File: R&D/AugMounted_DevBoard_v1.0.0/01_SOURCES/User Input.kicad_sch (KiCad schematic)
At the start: 25 parts, among them J501 J_0788641001_PAD, J502 J_0788641001, J503 J_0788641001, J504 J_0788641001_PAD, SW501 SW_SKRTLAE010, U502 ICS‐41350

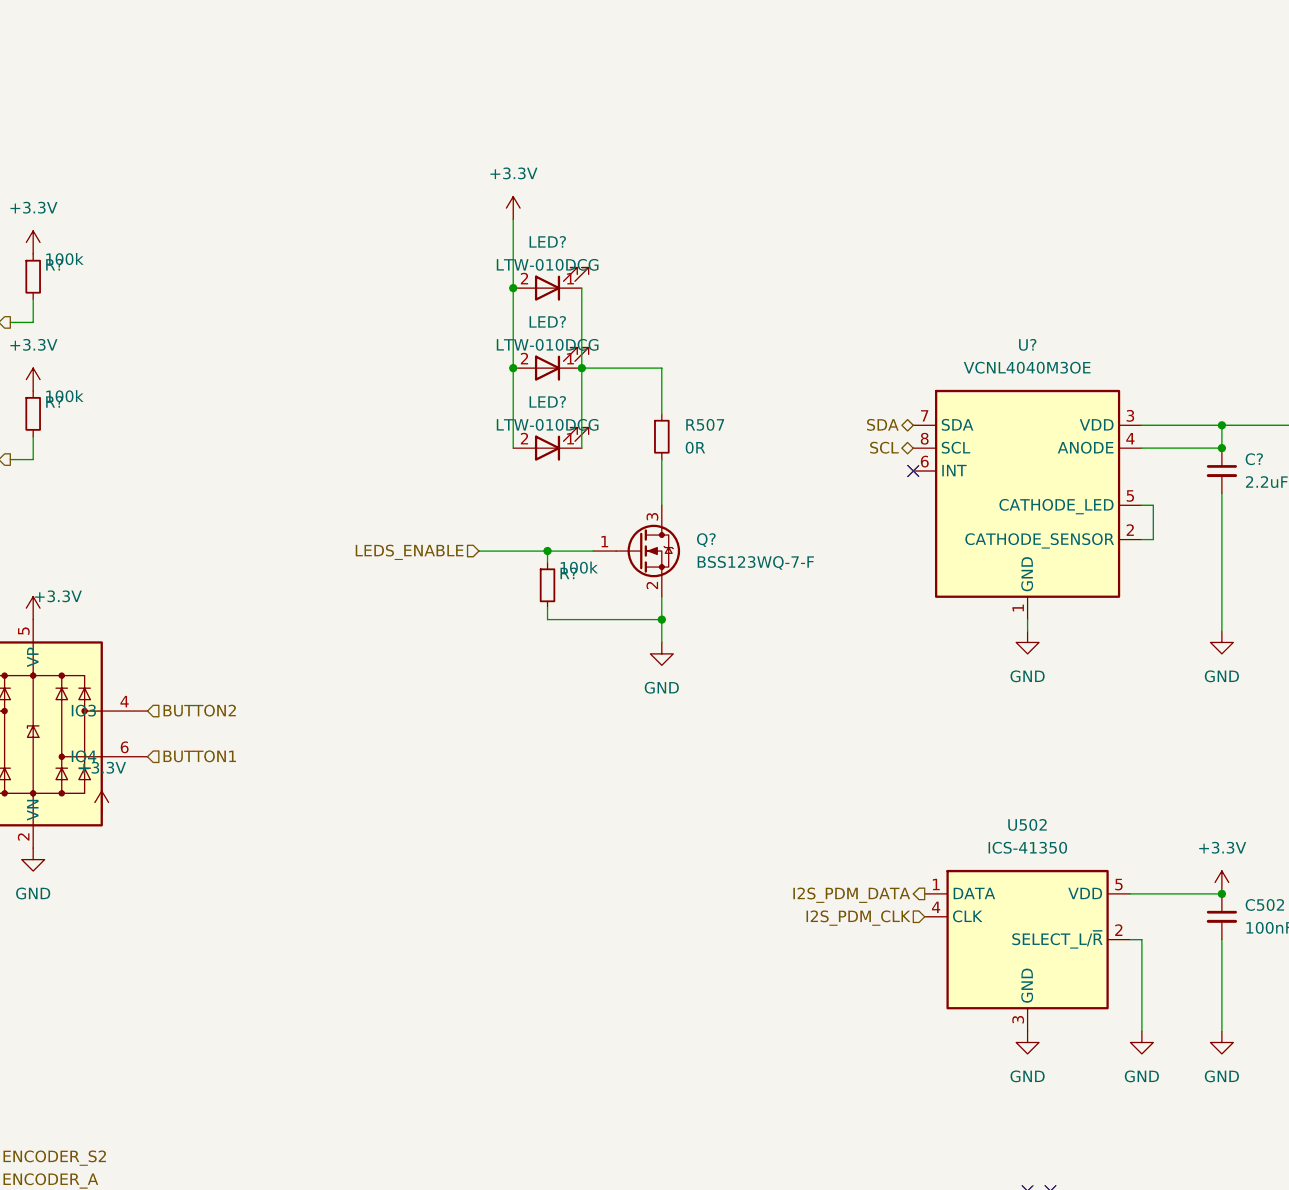
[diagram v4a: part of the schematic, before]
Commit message: Component layout is done, routing video signals is done too.
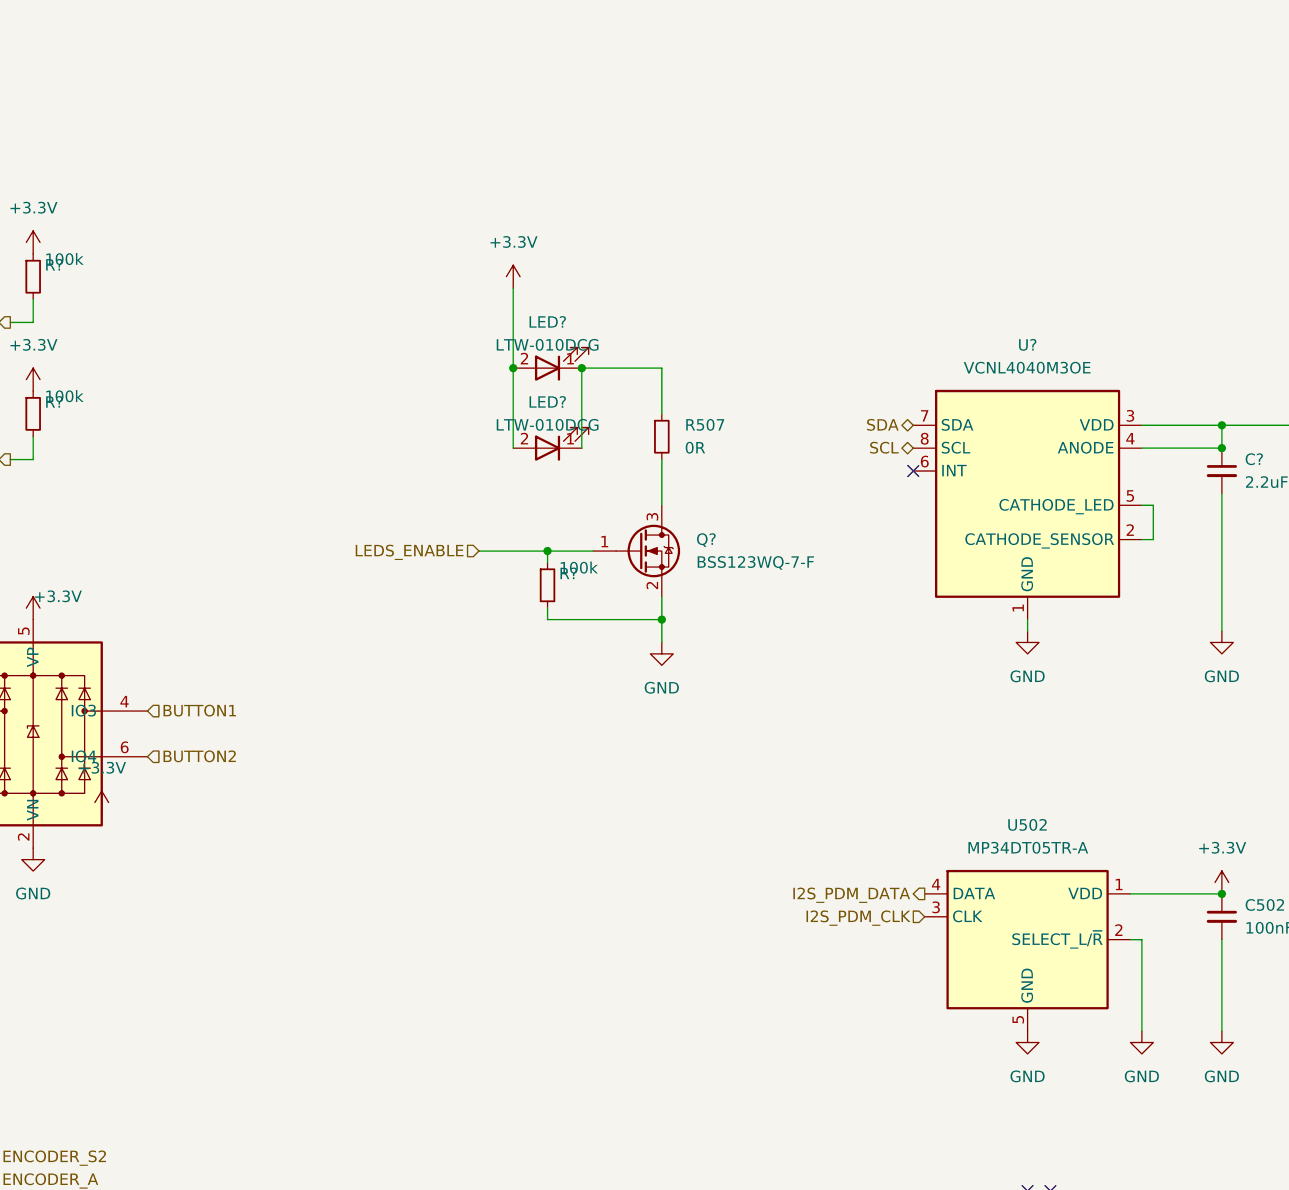
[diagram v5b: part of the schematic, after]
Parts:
- removed LED?: LED_LTW-010DCG, .mounted-lib:LED_LTW-010DCG, symbol .mounted-lib:LED_LTW-010DCG
- U502: value ICS‐41350 -> MP34DT05TR-A; footprint .mounted-lib:U_ICS-41350 -> .mounted-lib:U_MP34DT05TR-A; symbol .mounted-lib:U_ICS‐41350 -> .mounted-lib:U_MP34DT05TR-A; DisplayValue ICS‐41350 -> MP34DT05TR-A; MPN ICS‐41350 -> MP34DT05TR-A; Manufacturer TDK -> ST; MaxHeight_mm 0.98mm -> 1mm; Package ICS -> HCLGA
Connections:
- net +3.3V: now also U502.1 (VDD); no longer U502.5 (VDD)
- net BUTTON1: now also D502.4 (IO3); no longer D502.6 (IO4)
- net BUTTON2: now also D502.6 (IO4); no longer D502.4 (IO3)
- net GND: now also U502.5 (GND); no longer U502.3 (GND)
- net I2S_PDM_CLK: now also U502.3 (CLK); no longer U502.4 (CLK)
- net I2S_PDM_DATA: now also U502.4 (DATA); no longer U502.1 (DATA)
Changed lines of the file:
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@@
   (junction (at 234.95 139.7) (diameter 0) (color 0 0 0 0)
-  )
-  (junction (at 153.67 33.02) (diameter 0) (color 0 0 0 0)
   )
   (junction (at 212.09 158.75) (diameter 0) (color 0 0 0 0)
@@
     (stroke (width 0) (type default))
   )
-  (wire (pts (xy 153.67 25.4) (xy 153.67 33.02))
-    (stroke (width 0) (type default))
-  )
   (wire (pts (xy 232.41 48.26) (xy 232.41 50.8))
     (stroke (width 0) (type default))
@@
   )
   (wire (pts (xy 222.25 105.41) (xy 223.52 105.41))
-    (stroke (width 0) (type default))
-  )
-  (wire (pts (xy 161.29 33.02) (xy 161.29 41.91))
     (stroke (width 0) (type default))
   )
@@
     (effects (font (size 1.27 1.27)) (justify right))
   )
-  (hierarchical_label "BUTTON1" (shape input) (at 113.03 85.09 0) (fields_autoplaced)
+  (hierarchical_label "BUTTON1" (shape input) (at 113.03 80.01 0) (fields_autoplaced)
     (effects (font (size 1.27 1.27)) (justify left))
   )
@@
     (effects (font (size 1.27 1.27)) (justify right))
   )
-  (hierarchical_label "BUTTON2" (shape input) (at 113.03 80.01 0) (fields_autoplaced)
+  (hierarchical_label "BUTTON2" (shape input) (at 113.03 85.09 0) (fields_autoplaced)
     (effects (font (size 1.27 1.27)) (justify left))
   )
@@
     )
   )
-  (symbol (lib_id ".mounted-lib:U_ICS‐41350") (at 210.82 105.41 0) (unit 1)
+  (symbol (lib_id ".mounted-lib:U_MP34DT05TR-A") (at 210.82 105.41 0) (unit 1)
     (in_bom yes) (on_board yes) (dnp no) (fields_autoplaced)
     (property "Reference" "U502" (at 210.82 92.71 0)
       (effects (font (size 1.27 1.27)))
     )
-    (property "Value" "ICS‐41350" (at 251.46 92.71 0)
-      (effects (font (size 1.27 1.27)) (justify left) hide)
-    )
-    (property "Footprint" ".mounted-lib:U_ICS-41350" (at 251.46 94.615 0)
-      (effects (font (size 1.27 1.27)) (justify left) hide)
-    )
-    (property "Datasheet" "https://invensense.tdk.com/wp-content/uploads/2016/02/DS-000047-ICS-41350-v1.1.pdf" (at 251.46 96.52 0)
-      (effects (font (size 1.27 1.27)) (justify left) hide)
-    )
-    (property "Manufacturer" "TDK" (at 251.46 98.425 0)
-      (effects (font (size 1.27 1.27)) (justify left) hide)
-    )
-    (property "MPN" "ICS‐41350" (at 251.46 100.33 0)
-      (effects (font (size 1.27 1.27)) (justify left) hide)
-    )
-    (property "DisplayValue" "ICS‐41350" (at 210.82 95.25 0)
+    (property "Value" "MP34DT05TR-A" (at 251.46 92.71 0)
+      (effects (font (size 1.27 1.27)) (justify left) hide)
+    )
+    (property "Footprint" ".mounted-lib:U_MP34DT05TR-A" (at 251.46 94.615 0)
+      (effects (font (size 1.27 1.27)) (justify left) hide)
+    )
+    (property "Datasheet" "https://www.st.com/content/ccc/resource/technical/document/datasheet/group3/c7/90/d3/f6/b7/e7/40/c8/DM00415595/files/DM00415595.pdf/jcr:content/translations/en.DM00415595.pdf" (at 251.46 96.52 0)
+      (effects (font (size 1.27 1.27)) (justify left) hide)
+    )
+    (property "Manufacturer" "ST" (at 251.46 98.425 0)
+      (effects (font (size 1.27 1.27)) (justify left) hide)
+    )
+    (property "MPN" "MP34DT05TR-A" (at 251.46 100.33 0)
+      (effects (font (size 1.27 1.27)) (justify left) hide)
+    )
+    (property "DisplayValue" "MP34DT05TR-A" (at 210.82 95.25 0)
       (effects (font (size 1.27 1.27)))
     )
@@
       (effects (font (size 1.27 1.27)) (justify left) hide)
     )
-    (property "Package" "ICS" (at 251.46 115.57 0)
+    (property "Package" "HCLGA" (at 251.46 115.57 0)
       (effects (font (size 1.27 1.27)) (justify left) hide)
     )
@@
       (effects (font (size 1.27 1.27)) (justify left) hide)
     )
-    (property "MaxHeight_mm" "0.98mm" (at 251.46 125.095 0)
-      (effects (font (size 1.27 1.27)) (justify left) hide)
-    )
+    (property "MaxHeight_mm" "1mm" (at 251.46 125.095 0)
+      (effects (font (size 1.27 1.27)) (justify left) hide)
+    )
+    (pin "1")
     (pin "2")
     (pin "3")
+    (pin "5")
     (pin "4")
-    (pin "5")
-    (pin "1")
     (instances
       (project "AugMounted_DevBoard"
@@
     )
   )
-  (symbol (lib_id ".mounted-lib:LED_LTW-010DCG") (at 157.48 33.02 0) (unit 1)
-    (in_bom yes) (on_board yes) (dnp no)
-    (property "Reference" "LED?" (at 157.48 27.94 0)
-      (effects (font (size 1.27 1.27)))
-    )
-    (property "Value" "LED_LTW-010DCG" (at 198.12 20.32 0)
-      (effects (font (size 1.27 1.27)) (justify left) hide)
-    )
-    (property "Footprint" ".mounted-lib:LED_LTW-010DCG" (at 198.12 22.225 0)
-      (effects (font (size 1.27 1.27)) (justify left) hide)
-    )
-    (property "Datasheet" "https://optoelectronics.liteon.com/upload/download/DS22-2010-0013/LTW-010DCG%20DS_171030.PDF" (at 198.12 24.13 0)
-      (effects (font (size 1.27 1.27)) (justify left) hide)
-    )
-    (property "Manufacturer" "Lite-On" (at 198.12 26.035 0)
-      (effects (font (size 1.27 1.27)) (justify left) hide)
-    )
-    (property "MPN" "LTW-010DCG" (at 198.12 27.94 0)
-      (effects (font (size 1.27 1.27)) (justify left) hide)
-    )
-    (property "DisplayValue" "LTW-010DCG" (at 157.48 30.48 0)
-      (effects (font (size 1.27 1.27)))
-    )
-    (property "CMP_ID" "1089" (at 198.12 29.845 0)
-      (effects (font (size 1.27 1.27)) (justify left) hide)
-    )
-    (property "Category" "DIODE" (at 198.12 31.75 0)
-      (effects (font (size 1.27 1.27)) (justify left) hide)
-    )
-    (property "Family" "LED" (at 198.12 33.655 0)
-      (effects (font (size 1.27 1.27)) (justify left) hide)
-    )
-    (property "_Created" "JCN 2023-11-21" (at 198.12 35.56 0)
-      (effects (font (size 1.27 1.27)) (justify left) hide)
-    )
-    (property "_Checked" "" (at 198.12 37.465 0)
-      (effects (font (size 1.27 1.27)) (justify left) hide)
-    )
-    (property "_Confirmed" "" (at 198.12 39.37 0)
-      (effects (font (size 1.27 1.27)) (justify left) hide)
-    )
-    (property "Mount" "SMD" (at 198.12 41.275 0)
-      (effects (font (size 1.27 1.27)) (justify left) hide)
-    )
-    (property "Package" "LTW-010" (at 198.12 43.18 0)
-      (effects (font (size 1.27 1.27)) (justify left) hide)
-    )
-    (property "PartStatus" "" (at 198.12 45.085 0)
-      (effects (font (size 1.27 1.27)) (justify left) hide)
-    )
-    (property "TempMin_C" "-30°C" (at 198.12 46.99 0)
-      (effects (font (size 1.27 1.27)) (justify left) hide)
-    )
-    (property "TempMax_C" "+85°C" (at 198.12 48.895 0)
-      (effects (font (size 1.27 1.27)) (justify left) hide)
-    )
-    (property "Automotive" "N" (at 198.12 50.8 0)
-      (effects (font (size 1.27 1.27)) (justify left) hide)
-    )
-    (property "MaxHeight_mm" "0.4mm" (at 198.12 52.705 0)
-      (effects (font (size 1.27 1.27)) (justify left) hide)
-    )
-    (pin "1")
-    (pin "2")
-    (instances
-      (project "AugMounted_DevBoard"
-        (path "/75b08848-9393-425e-a17d-60105119a7b1/a7e357a9-82a1-4b8d-acf0-65ce824c3be5"
-          (reference "LED?") (unit 1)
-        )
-        (path "/75b08848-9393-425e-a17d-60105119a7b1/2b4b9f93-a38b-41c6-bf78-4a8e57625d62"
-          (reference "LED501") (unit 1)
-        )
-      )
-    )
-  )
   (symbol (lib_id ".mounted-lib:D_SRV05-4") (at 38.1 82.55 0) (unit 1)
     (in_bom yes) (on_board yes) (dnp no)
@@
     )
   )
-  (symbol (lib_id "power:+3.3V") (at 153.67 25.4 0) (unit 1)
-    (in_bom yes) (on_board yes) (dnp no) (fields_autoplaced)
-    (property "Reference" "#PWR?" (at 153.67 29.21 0)
-      (effects (font (size 1.27 1.27)) hide)
-    )
-    (property "Value" "+3.3V" (at 153.67 20.32 0)
-      (effects (font (size 1.27 1.27)))
-    )
-    (property "Footprint" "" (at 153.67 25.4 0)
-      (effects (font (size 1.27 1.27)) hide)
-    )
-    (property "Datasheet" "" (at 153.67 25.4 0)
-      (effects (font (size 1.27 1.27)) hide)
-    )
+  (symbol (lib_id "power:+3.3V") (at 153.67 33.02 0) (unit 1)
+    (in_bom yes) (on_board yes) (dnp no) (fields_autoplaced)
+    (property "Reference" "#PWR?" (at 153.67 36.83 0)
+      (effects (font (size 1.27 1.27)) hide)
+    )
+    (property "Value" "+3.3V" (at 153.67 27.94 0)
+      (effects (font (size 1.27 1.27)))
+    )
+    (property "Footprint" "" (at 153.67 33.02 0)
+      (effects (font (size 1.27 1.27)) hide)
+    )
+    (property "Datasheet" "" (at 153.67 33.02 0)
+      (effects (font (size 1.27 1.27)) hide)
+    )
